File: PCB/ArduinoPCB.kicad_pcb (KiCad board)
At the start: 2 copper layers, 28 parts, among them J1 Ext. Conn, J10 Reed2, J11 EndStop2, J12 PCA9685, J13 EndStop3, J14 Reed3, J15 Reed4, J2 StepVCC, J3 StepGND, J4 Stepper1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

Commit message: Rev2 of PCB
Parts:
- added REF**: M3, Mounting_Holes:MountingHole_3.2mm_M3, F.Cu at (229.9, 47.0)
- added REF**: M3, Mounting_Holes:MountingHole_3.2mm_M3, F.Cu at (232.4, 135.9)
- added REF**: M3, Mounting_Holes:MountingHole_3.2mm_M3, F.Cu at (119.4, 128.3)
- added REF**: M3, Mounting_Holes:MountingHole_3.2mm_M3, F.Cu at (146.1, 54.6)
- moved J6 133.2 mm to (146.1, 137.2), turned to 180 degrees
- moved J10 126.1 mm to (171.4, 137.2), turned to 180 degrees
- moved U1 104.2 mm to (137.2, 133.3), turned to 180 degrees
- moved U2 103.3 mm to (162.6, 133.3), turned to 180 degrees
- moved J14 101.6 mm to (200.7, 137.2), turned to 180 degrees
- moved J15 82.6 mm to (226.1, 137.2), turned to 180 degrees
- moved U3 69.9 mm to (191.8, 133.3)
- moved R2 64.8 mm to (205.7, 115.6)
- moved R1 63.7 mm to (151.1, 113.0), turned to 90 degrees
- moved J1 58.3 mm to (121.9, 115.6), turned to 180 degrees
- moved U4 50.8 mm to (217.2, 133.3)
- moved J3 29.0 mm to (229.9, 77.5)
- moved C1 25.4 mm to (228.6, 69.8), turned to 270 degrees
- moved J9 15.3 mm to (143.5, 69.8)
- moved A2 12.7 mm to (130.8, 72.4)
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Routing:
- net 3V3: track 6.13 -> 62.8 mm
- net GND: track 385.2 -> 437.5 mm, vias 0 -> 3
- net SCL: track 228.9 -> 278.7 mm
- net SDA: track 223.7 -> 270.0 mm
- net Pullup2: track 96.8 -> 66.8 mm
- net Net-(J6-Pad5): track 14.8 -> 42.9 mm
- net Net-(J14-Pad5): track 14.8 -> 42.9 mm
- net Net-(J15-Pad5): track 14.8 -> 42.9 mm
- net Net-(J10-Pad5): track 14.8 -> 42.9 mm
- net Net-(J6-Pad6): track 12.3 -> 39.3 mm
- net Net-(J10-Pad6): track 12.3 -> 39.3 mm
- net Net-(J15-Pad6): track 12.3 -> 39.3 mm
- net Net-(J14-Pad6): track 12.3 -> 39.3 mm
- net 8V_GND: track 137.5 -> 111.0 mm
- net Net-(J15-Pad7): track 9.72 -> 35.7 mm
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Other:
- board text added: "© 2019 Viperinius/Chess-Robot Rev.2"

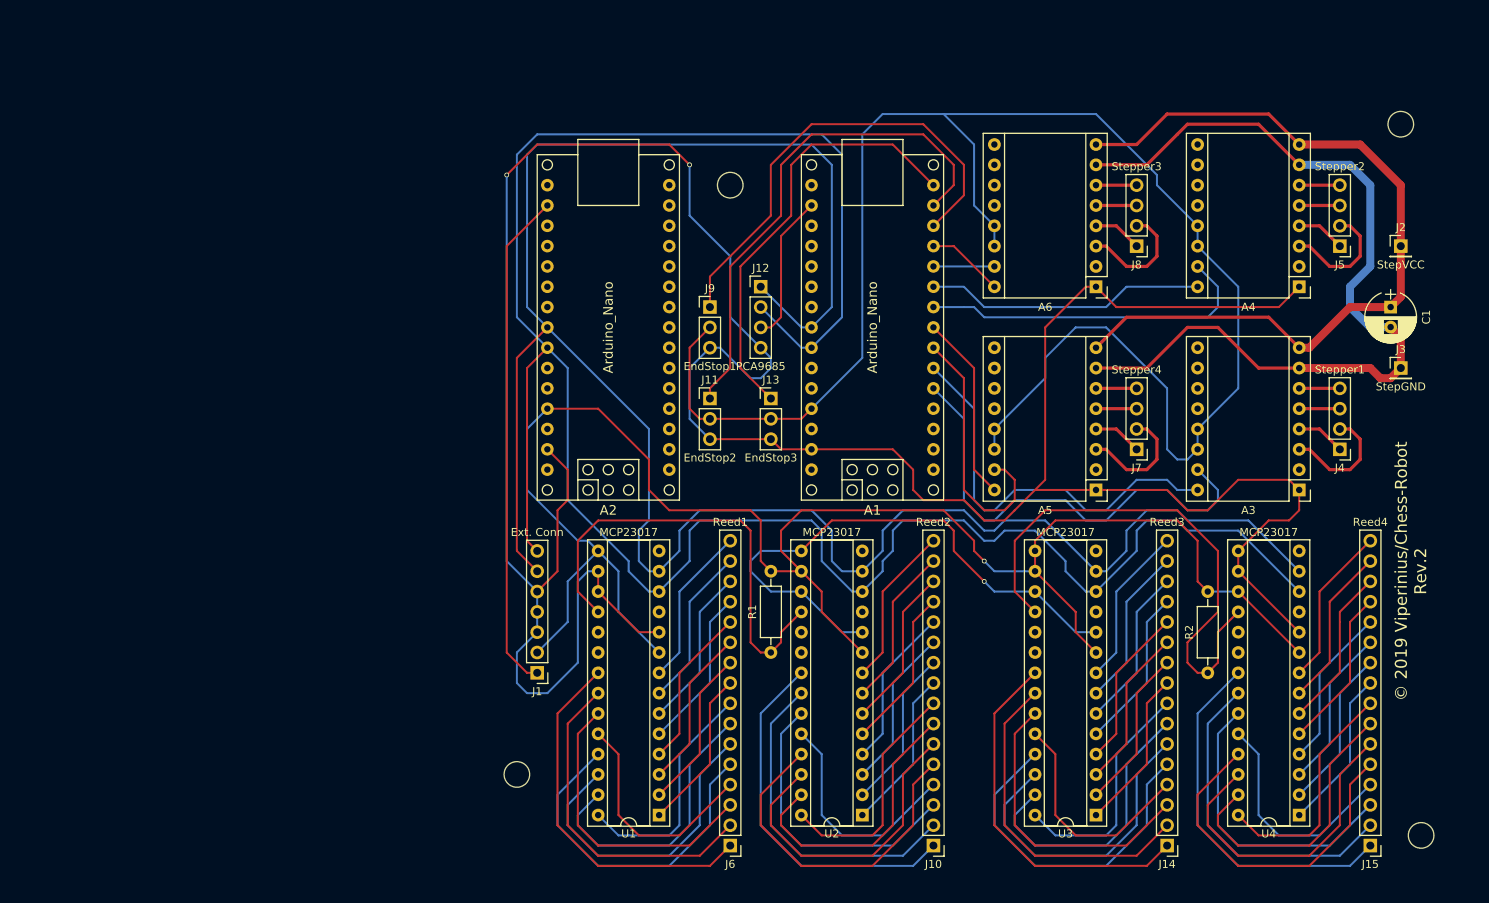
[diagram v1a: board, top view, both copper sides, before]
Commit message: minimal PCB changes to be able to manufacture it, added image
Signed-off-by: Viperinius <41393831+Viperinius@users.noreply.github.com>
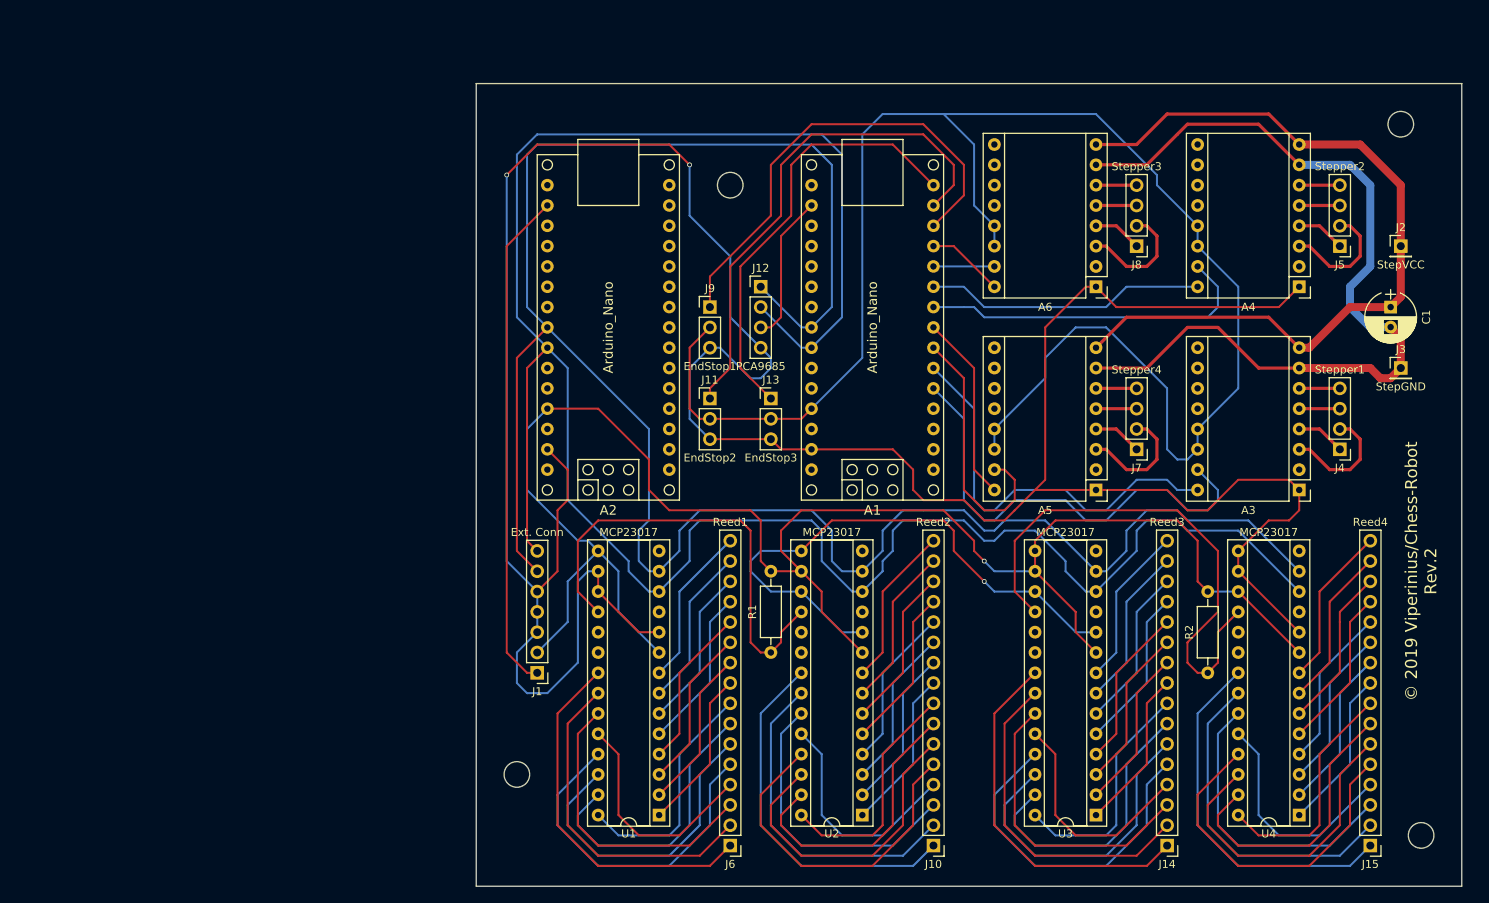
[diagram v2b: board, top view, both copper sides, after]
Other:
- board outline added: 123.2 x 100.3 mm
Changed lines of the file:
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@@
     (area 115.704999 43.314999 236.085001 141.165)
     (thickness 1.6)
-    (drawings 1)
+    (drawings 5)
     (tracks 734)
     (zones 0)
@@
     (pad 1 np_thru_hole circle (at 0 0) (size 3.2 3.2) (drill 3.2) (layers *.Cu *.Mask))
   )
-  (gr_text "© 2019 Viperinius/Chess-Robot\nRev.2" (at 231.14 102.87 90) (layer F.SilkS)
+  (gr_line (start 114.3 142.24) (end 237.49 142.24) (angle 90) (layer Edge.Cuts) (width 0.1))
+  (gr_line (start 114.3 41.91) (end 114.3 142.24) (angle 90) (layer Edge.Cuts) (width 0.1))
+  (gr_line (start 237.49 41.91) (end 114.3 41.91) (angle 90) (layer Edge.Cuts) (width 0.1))
+  (gr_line (start 237.49 142.24) (end 237.49 41.91) (angle 90) (layer Edge.Cuts) (width 0.1))
+  (gr_text "© 2019 Viperinius/Chess-Robot\nRev.2" (at 232.41 102.87 90) (layer F.SilkS)
     (effects (font (size 1.5 1.5) (thickness 0.3)))
   )
